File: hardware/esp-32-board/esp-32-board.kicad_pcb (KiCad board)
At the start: 2 copper layers, 53.8 x 69.1 mm, 32 parts, among them J1 Conn_Arduino_UNO_R3, J2 Conn_02x03_Odd_Even, J3 ESP-PROG-Program, J4 ESP-PROG-Debug, J5 USB_B_Micro, J6 Barrel_Jack_MountingPin, Q1 BCR129S, SW1 SW_Push, SW2 SW_Push, SW3 SW_DPDT_x2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

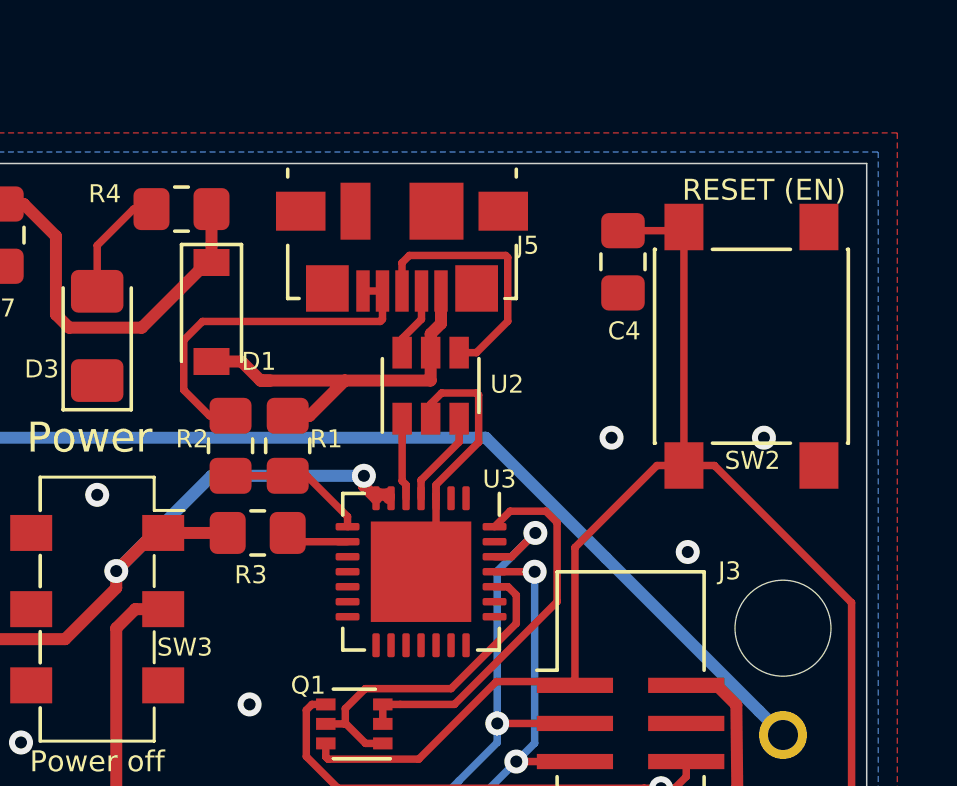
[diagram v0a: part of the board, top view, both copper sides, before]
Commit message: Update USB connector
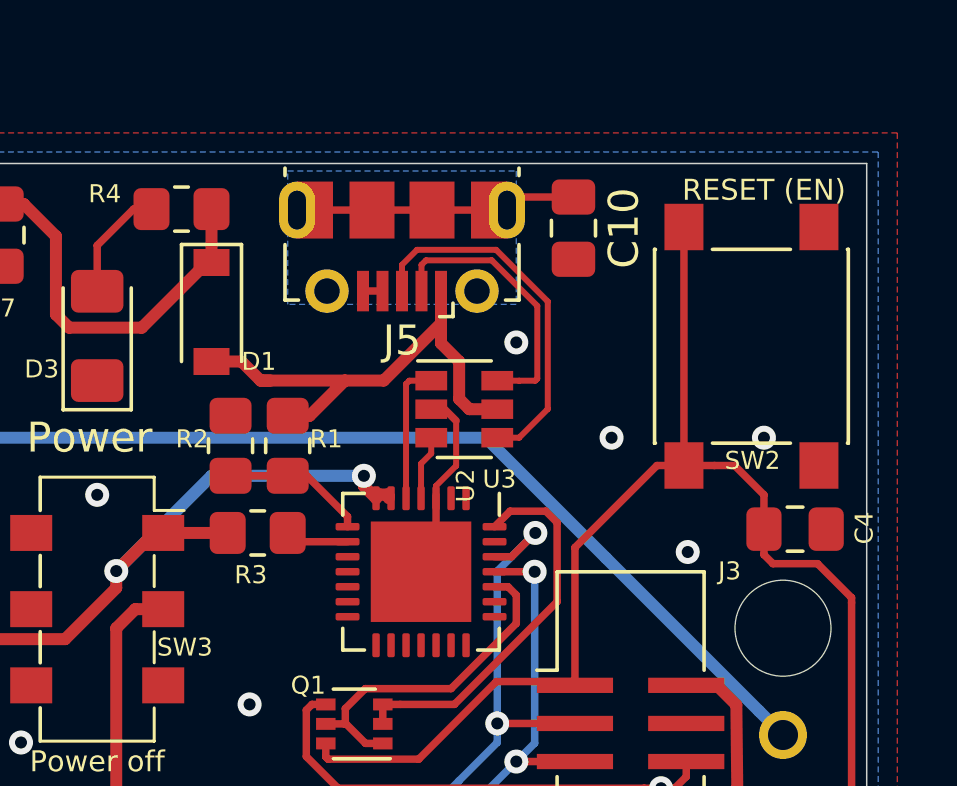
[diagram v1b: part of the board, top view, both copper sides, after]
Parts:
- added C10: 22uF, Capacitor_SMD:C_0805_2012Metric_Pad1.18x1.45mm_HandSolder, F.Cu at (173.4, 23.5)
- J5: footprint Connector_USB:USB_Micro-B_Molex_47346-0001 -> Connector_USB:USB_Micro-B_Molex-105017-0001
- moved C4 10.6 mm to (180.7, 33.5), turned to 180 degrees
- moved U2 1.37 mm to (169.7, 29.5), turned to 0 degrees
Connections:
- J5 pad 6: (no net) -> Net-(C10-Pad1)
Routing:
- net GND: track 32.7 -> 18.8 mm
- net Net-(C10-Pad1): track 0.00 -> 8.20 mm
- net Net-(J5-Pad2): track 2.32 -> 9.21 mm
- net Net-(J5-Pad3): track 8.78 -> 12.3 mm
- net /USB/VBUS: track 13.4 -> 16.7 mm
- net /USB/USB_DN: track 2.71 -> 4.69 mm
- net /USB/USB_DP: track 3.18 -> 2.16 mm
- net /EN: track 115.0 -> 114.2 mm
- net (no net): vias 0 -> 1
- added copper zone on B.Cu, net Net-(C10-Pad1)
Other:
- net class USB Data added: clearance 0.15, trace_width 0.2, via_dia 0.8, via_drill 0.4

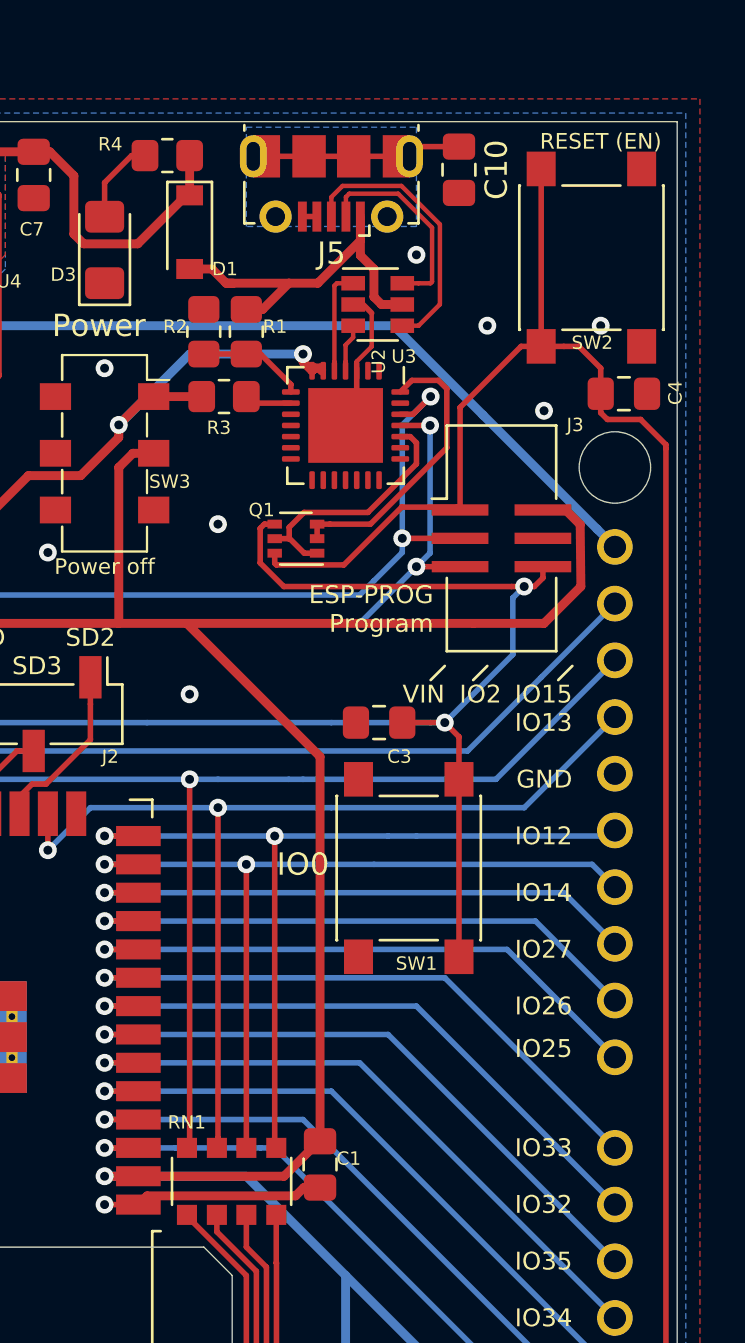
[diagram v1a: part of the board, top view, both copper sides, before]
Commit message: Change microUSB
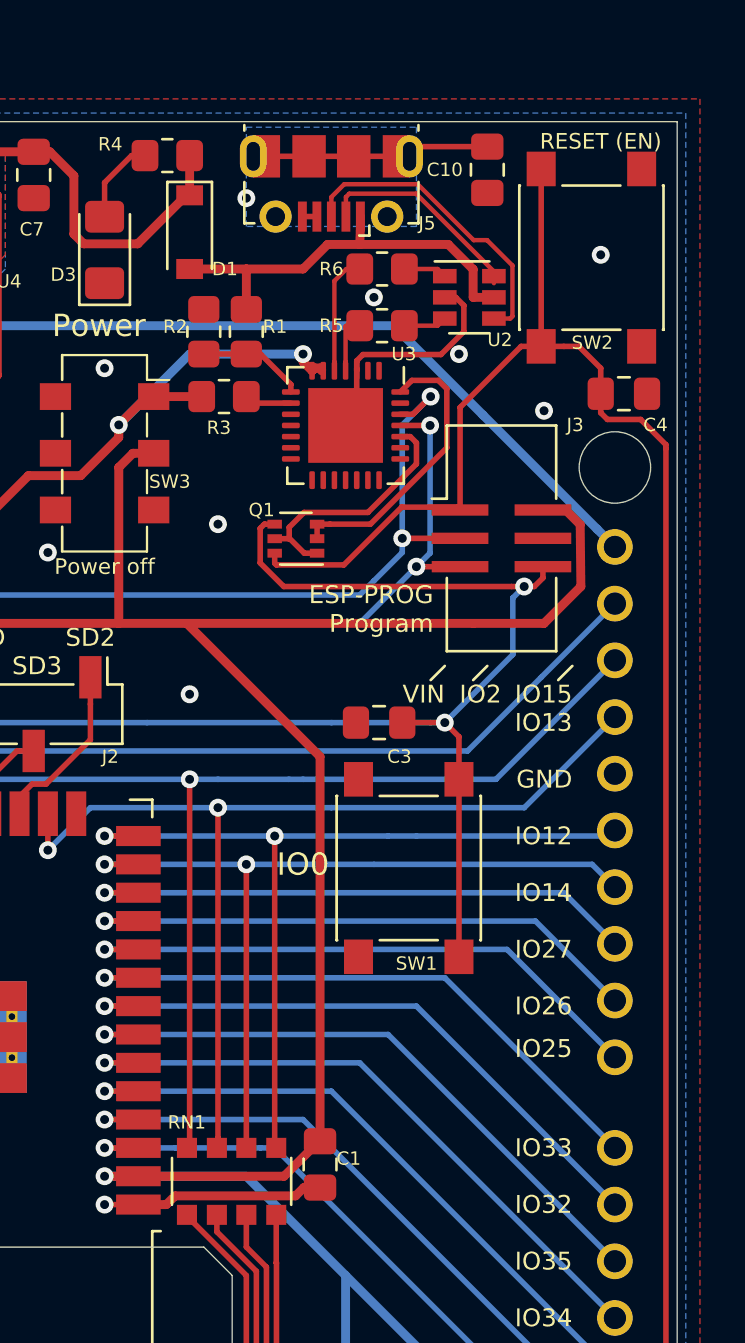
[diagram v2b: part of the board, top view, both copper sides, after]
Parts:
- added R5: 22 Ohm, Resistor_SMD:R_0805_2012Metric_Pad1.20x1.40mm_HandSolder, F.Cu at (169.9, 30.5)
- added R6: 22 Ohm, Resistor_SMD:R_0805_2012Metric_Pad1.20x1.40mm_HandSolder, F.Cu at (169.9, 27.9)
- moved U2 4.12 mm to (173.8, 29.2)
- moved C10 1.27 mm to (174.6, 23.5)
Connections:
- U2 pad 1: /USB/USB_DN -> Net-(R6-Pad1)
- U2 pad 3: /USB/USB_DP -> Net-(R5-Pad1)
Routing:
- net GND: track 18.8 -> 22.9 mm, vias 16 -> 18
- net /USB/VBUS: track 16.7 -> 18.9 mm
- net Net-(R6-Pad1): track 0.00 -> 1.94 mm
- net Net-(R5-Pad1): track 0.00 -> 1.94 mm
- net Net-(J5-Pad3): track 12.3 -> 13.9 mm
- net Net-(C10-Pad1): track 8.20 -> 9.47 mm
- net /USB/USB_DN: track 4.69 -> 5.38 mm
- net (no net): vias 1 -> 0

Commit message: Fix auto-reset circuit connections
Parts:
- moved Q1 0.32 mm to (166.4, 40.0), turned to 0 degrees
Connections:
- Q1 pad 3: /USB/DTR -> /IO0
- Q1 pad 4: /IO0 -> /USB/DTR
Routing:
- net /IO0: track 81.1 -> 78.3 mm
- net /USB/RTS: track 11.3 -> 9.46 mm
- net /USB/DTR: track 13.0 -> 14.7 mm
- net /EN: track 114.2 -> 113.8 mm, vias 1 -> 3

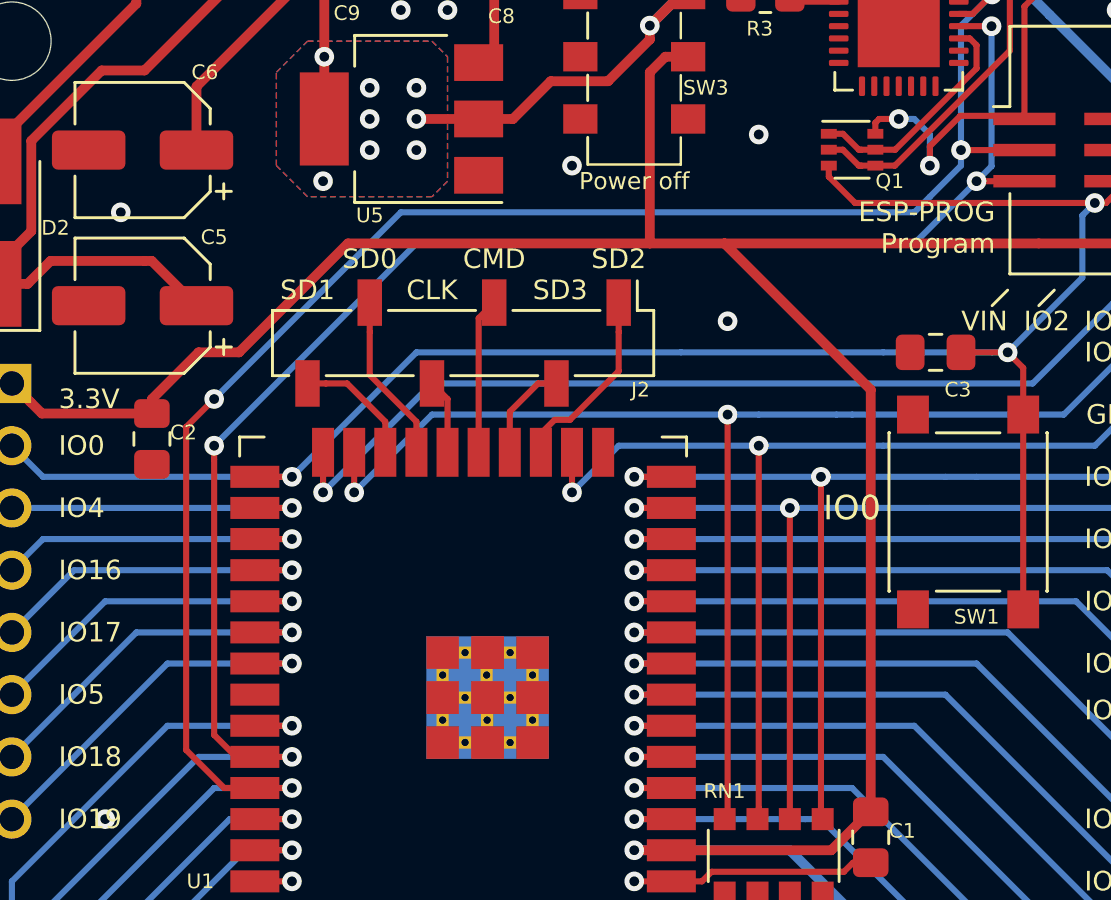
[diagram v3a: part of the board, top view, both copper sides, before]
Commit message: Use THT connector for pins 17-21
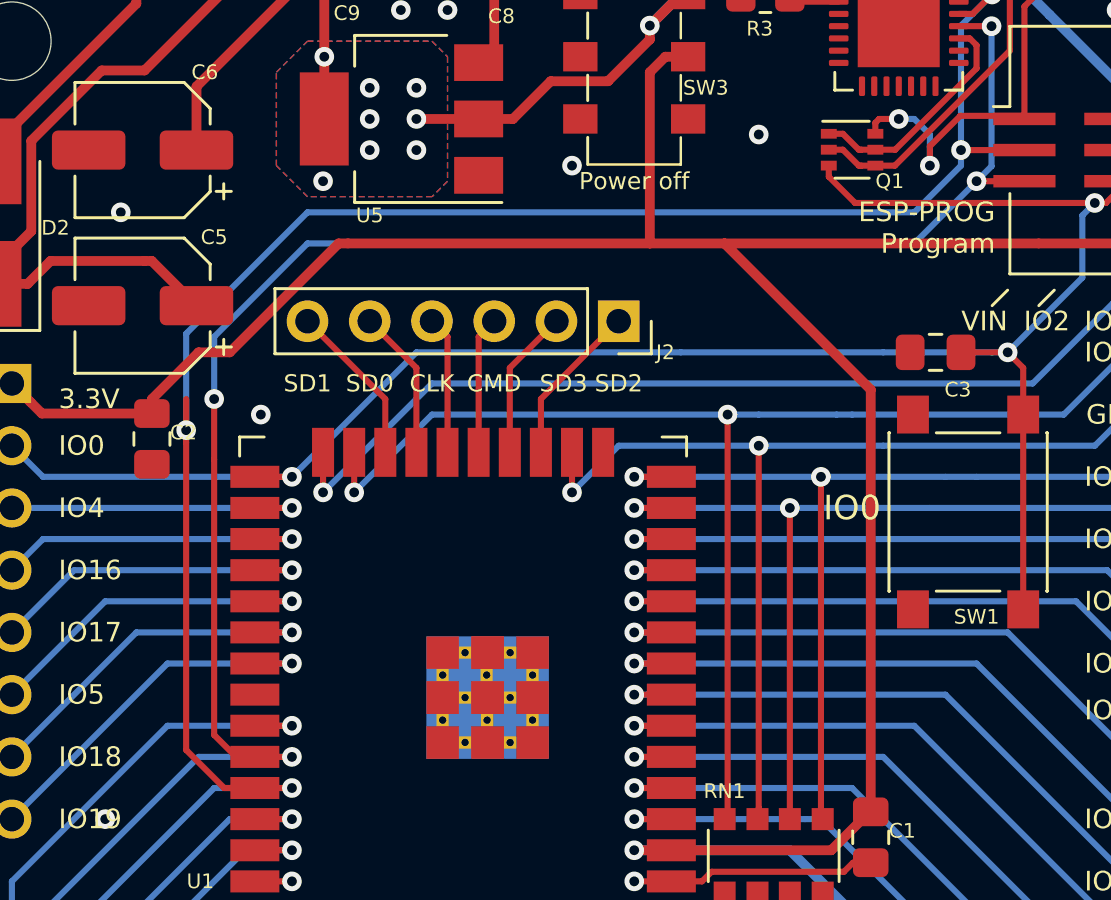
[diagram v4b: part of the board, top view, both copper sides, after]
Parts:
- J2: footprint Connector_PinSocket_2.54mm:PinSocket_1x06_P2.54mm_Vertical_SMD_Pin1Left -> Connector_PinSocket_2.54mm:PinSocket_1x06_P2.54mm_Vertical
- moved J2 6.41 mm to (156.8, 47.0)
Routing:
- net /TXD0: track 84.0 -> 87.5 mm
- net /RXD0: track 77.9 -> 80.5 mm
- net /CLK: track 3.07 -> 5.61 mm
- net /SD3: track 4.04 -> 6.14 mm
- net /SD1: track 5.07 -> 6.67 mm
- net /SD2: track 7.79 -> 6.67 mm
- net /SD0: track 6.90 -> 6.14 mm
- net /CMD: track 6.37 -> 5.61 mm

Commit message: Layout optimization
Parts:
- moved SW3 0.63 mm to (157.5, 36.8)
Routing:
- net +3V3: track 149.1 -> 146.5 mm
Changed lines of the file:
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@@
     (thickness 1.6)
     (drawings 64)
-    (tracks 554)
+    (tracks 559)
     (zones 0)
     (modules 35)
@@
   )
   (module Button_Switch_SMD:Nidec_CL-SB-22B-0X (layer F.Cu)
-    (at 157.48 36.195 270)
+    (at 157.48 36.83 270)
     (fp_text reference SW3 (at 1.27 -2.921 180) (layer F.SilkS)
       (effects (font (size 0.6 0.6) (thickness 0.15)))
@@
   (gr_line (start 137.795 73.025) (end 137.795 81.28) (layer Edge.Cuts) (width 0.05))
   (gr_line (start 139.065 71.755) (end 137.795 73.025) (layer Edge.Cuts) (width 0.05))
-  (gr_text "Power off" (at 157.48 41.275) (layer F.SilkS)
+  (gr_text "Power off" (at 157.48 41.91) (layer F.SilkS)
     (effects (font (size 0.7 0.7) (thickness 0.175)))
   )
-  (gr_text Power (at 157.226 30.48) (layer F.SilkS)
+  (gr_text Power (at 157.226 31.115) (layer F.SilkS)
     (effects (font (size 1 1) (thickness 0.25)))
   )
@@
   (via (at 157.48 68.58) (size 0.8) (drill 0.4) (layers F.Cu B.Cu) (net 3))
   (segment (start 157.48 68.58) (end 163.83 68.58) (width 0.4) (layer B.Cu) (net 3))
-  (segment (start 168.275 73.025) (end 168.275 80.645) (width 0.4) (layer B.Cu) (net 3))
-  (segment (start 168.275 73.025) (end 180.34 85.09) (width 0.4) (layer B.Cu) (net 3))
   (segment (start 163.83 68.58) (end 168.275 73.025) (width 0.4) (layer B.Cu) (net 3))
-  (segment (start 164.415 84.505) (end 160.02 84.505) (width 0.4) (layer B.Cu) (net 3))
-  (segment (start 168.275 80.645) (end 164.415 84.505) (width 0.4) (layer B.Cu) (net 3))
-  (segment (start 158.115 36.83) (end 158.115 43.815) (width 0.4) (layer F.Cu) (net 3))
-  (segment (start 159.68 36.195) (end 158.75 36.195) (width 0.4) (layer F.Cu) (net 3))
-  (segment (start 158.115 36.83) (end 158.75 36.195) (width 0.4) (layer F.Cu) (net 3))
   (segment (start 158.115 43.815) (end 161.163 43.815) (width 0.4) (layer F.Cu) (net 3))
-  (segment (start 165.520002 68.58) (end 167.132 66.968002) (width 0.4) (layer F.Cu) (net 3))
-  (segment (start 158.995 68.58) (end 165.520002 68.58) (width 0.4) (layer F.Cu) (net 3))
-  (segment (start 167.132 66.968002) (end 167.132 66.548) (width 0.4) (layer F.Cu) (net 3))
-  (segment (start 167.132 49.784) (end 161.163 43.815) (width 0.4) (layer F.Cu) (net 3))
-  (segment (start 167.132 66.548) (end 167.132 49.784) (width 0.4) (layer F.Cu) (net 3))
   (segment (start 178.131 38.735) (end 178.785 39.389) (width 0.4) (layer F.Cu) (net 3))
   (segment (start 178.785 39.389) (end 178.816 42.164) (width 0.4) (layer F.Cu) (net 3))
   (segment (start 177.115 38.735) (end 178.131 38.735) (width 0.4) (layer F.Cu) (net 3))
   (segment (start 178.816 42.164) (end 177.165 43.815) (width 0.4) (layer F.Cu) (net 3))
-  (segment (start 173.99 43.815) (end 161.163 43.815) (width 0.4) (layer F.Cu) (net 3))
   (segment (start 177.165 43.815) (end 173.99 43.815) (width 0.4) (layer F.Cu) (net 3))
   (segment (start 145.796 43.815) (end 158.115 43.815) (width 0.4) (layer F.Cu) (net 3))
@@
   (segment (start 139.7 48.26) (end 137.795 50.1695) (width 0.4) (layer F.Cu) (net 3))
   (segment (start 140.97 48.26) (end 145.415 43.815) (width 0.4) (layer F.Cu) (net 3))
+  (segment (start 167.132 66.968002) (end 167.132 66.548) (width 0.4) (layer F.Cu) (net 3))
+  (segment (start 158.995 68.58) (end 165.520002 68.58) (width 0.4) (layer F.Cu) (net 3))
+  (segment (start 165.520002 68.58) (end 167.132 66.968002) (width 0.4) (layer F.Cu) (net 3))
+  (segment (start 167.005 43.815) (end 167.132 43.942) (width 0.4) (layer F.Cu) (net 3))
+  (segment (start 173.99 43.815) (end 167.005 43.815) (width 0.4) (layer F.Cu) (net 3))
+  (segment (start 167.132 54.102) (end 167.132 67.013) (width 0.4) (layer F.Cu) (net 3))
+  (segment (start 167.132 53.467) (end 167.132 54.102) (width 0.4) (layer F.Cu) (net 3))
+  (segment (start 167.005 43.815) (end 161.29 43.815) (width 0.4) (layer F.Cu) (net 3))
+  (segment (start 161.29 43.815) (end 161.163 43.815) (width 0.4) (layer F.Cu) (net 3))
+  (segment (start 161.29 43.815) (end 161.29 47.625) (width 0.4) (layer F.Cu) (net 3))
+  (segment (start 161.29 47.625) (end 167.005 53.34) (width 0.4) (layer F.Cu) (net 3))
+  (segment (start 159.78 36.83) (end 161.29 38.34) (width 0.4) (layer F.Cu) (net 3))
+  (segment (start 159.68 36.83) (end 159.78 36.83) (width 0.4) (layer F.Cu) (net 3))
+  (segment (start 161.29 38.34) (end 161.29 43.815) (width 0.4) (layer F.Cu) (net 3))
+  (segment (start 165.685 84.505) (end 172.72 77.47) (width 0.4) (layer B.Cu) (net 3))
+  (segment (start 160.02 84.505) (end 165.685 84.505) (width 0.4) (layer B.Cu) (net 3))
+  (segment (start 168.275 73.025) (end 172.72 77.47) (width 0.4) (layer B.Cu) (net 3))
+  (segment (start 172.72 77.47) (end 180.34 85.09) (width 0.4) (layer B.Cu) (net 3))
   (segment (start 141.995 53.34) (end 143.51 53.34) (width 0.25) (layer F.Cu) (net 4))
   (segment (start 143.51 53.34) (end 143.51 53.34) (width 0.25) (layer F.Cu) (net 4))
@@
   (segment (start 137.49399 36.756008) (end 135.743736 36.756008) (width 0.4) (layer F.Cu) (net 41))
   (segment (start 174.4325 34.4825) (end 179.540001 39.590001) (width 0.4) (layer B.Cu) (net 41))
-  (segment (start 159.68 33.655) (end 161.83 33.655) (width 0.4) (layer F.Cu) (net 42))
   (segment (start 166.775 32.498) (end 166.37 32.093) (width 0.4) (layer F.Cu) (net 42))
   (segment (start 166.37 32.093) (end 166.37 31.75) (width 0.4) (layer F.Cu) (net 42))
   (segment (start 166.37 31.75) (end 166.37 31.75) (width 0.4) (layer F.Cu) (net 42))
   (segment (start 166.37 31.75) (end 166.37 31.75) (width 0.4) (layer F.Cu) (net 42))
-  (via (at 166.37 31.75) (size 0.8) (drill 0.4) (layers F.Cu B.Cu) (net 42))
-  (segment (start 158.115 34.925) (end 158.115 34.925) (width 0.4) (layer F.Cu) (net 42))
-  (segment (start 159.385 33.655) (end 159.68 33.655) (width 0.4) (layer F.Cu) (net 42))
-  (segment (start 158.115 34.925) (end 159.385 33.655) (width 0.4) (layer F.Cu) (net 42))
-  (via (at 158.115 34.925) (size 0.8) (drill 0.4) (layers F.Cu B.Cu) (net 42))
-  (segment (start 161.29 31.75) (end 166.37 31.75) (width 0.4) (layer B.Cu) (net 42))
-  (segment (start 158.115 34.925) (end 161.29 31.75) (width 0.4) (layer B.Cu) (net 42))
+  (via (at 158.115 35.56) (size 0.8) (drill 0.4) (layers F.Cu B.Cu) (net 42))
   (segment (start 167.19999 32.42299) (end 167.19999 32.498) (width 0.4) (layer F.Cu) (net 42))
   (segment (start 167.15 32.373) (end 167.19999 32.42299) (width 0.4) (layer F.Cu) (net 42))
@@
   (segment (start 144.83 38.735) (end 144.83 33.4825) (width 0.4) (layer F.Cu) (net 42))
   (segment (start 144.83 33.4825) (end 145.2925 33.02) (width 0.4) (layer F.Cu) (net 42))
-  (segment (start 158.115 35.490685) (end 158.115 34.925) (width 0.4) (layer F.Cu) (net 42))
-  (segment (start 156.410684 37.195001) (end 158.115 35.490685) (width 0.4) (layer F.Cu) (net 42))
-  (segment (start 154.069999 37.195001) (end 156.410684 37.195001) (width 0.4) (layer F.Cu) (net 42))
-  (segment (start 152.53 38.735) (end 154.069999 37.195001) (width 0.4) (layer F.Cu) (net 42))
-  (segment (start 151.13 38.735) (end 152.53 38.735) (width 0.4) (layer F.Cu) (net 42))
+  (segment (start 157.549315 35.56) (end 158.115 35.56) (width 0.4) (layer F.Cu) (net 42))
+  (segment (start 154.555 35.56) (end 157.549315 35.56) (width 0.4) (layer F.Cu) (net 42))
+  (segment (start 151.38 38.735) (end 154.555 35.56) (width 0.4) (layer F.Cu) (net 42))
+  (segment (start 151.13 38.735) (end 151.38 38.735) (width 0.4) (layer F.Cu) (net 42))
+  (segment (start 159.385 34.29) (end 159.68 34.29) (width 0.4) (layer F.Cu) (net 42))
+  (segment (start 158.115 35.56) (end 159.385 34.29) (width 0.4) (layer F.Cu) (net 42))
+  (segment (start 166.37 31.75) (end 166.37 31.75) (width 0.4) (layer F.Cu) (net 42))
+  (via (at 166.37 31.75) (size 0.8) (drill 0.4) (layers F.Cu B.Cu) (net 42))
+  (segment (start 161.925 31.75) (end 158.115 35.56) (width 0.4) (layer B.Cu) (net 42))
+  (segment (start 166.37 31.75) (end 161.925 31.75) (width 0.4) (layer B.Cu) (net 42))
+  (segment (start 160.315 33.655) (end 159.68 34.29) (width 0.4) (layer F.Cu) (net 42))
+  (segment (start 161.83 33.655) (end 160.315 33.655) (width 0.4) (layer F.Cu) (net 42))
   (segment (start 137.16 33.75) (end 137.16 31.75) (width 0.4) (layer F.Cu) (net 43))
   (segment (start 137.16 34.028) (end 137.16 33.75) (width 0.4) (layer F.Cu) (net 43))
